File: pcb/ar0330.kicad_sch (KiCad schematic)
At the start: 37 parts

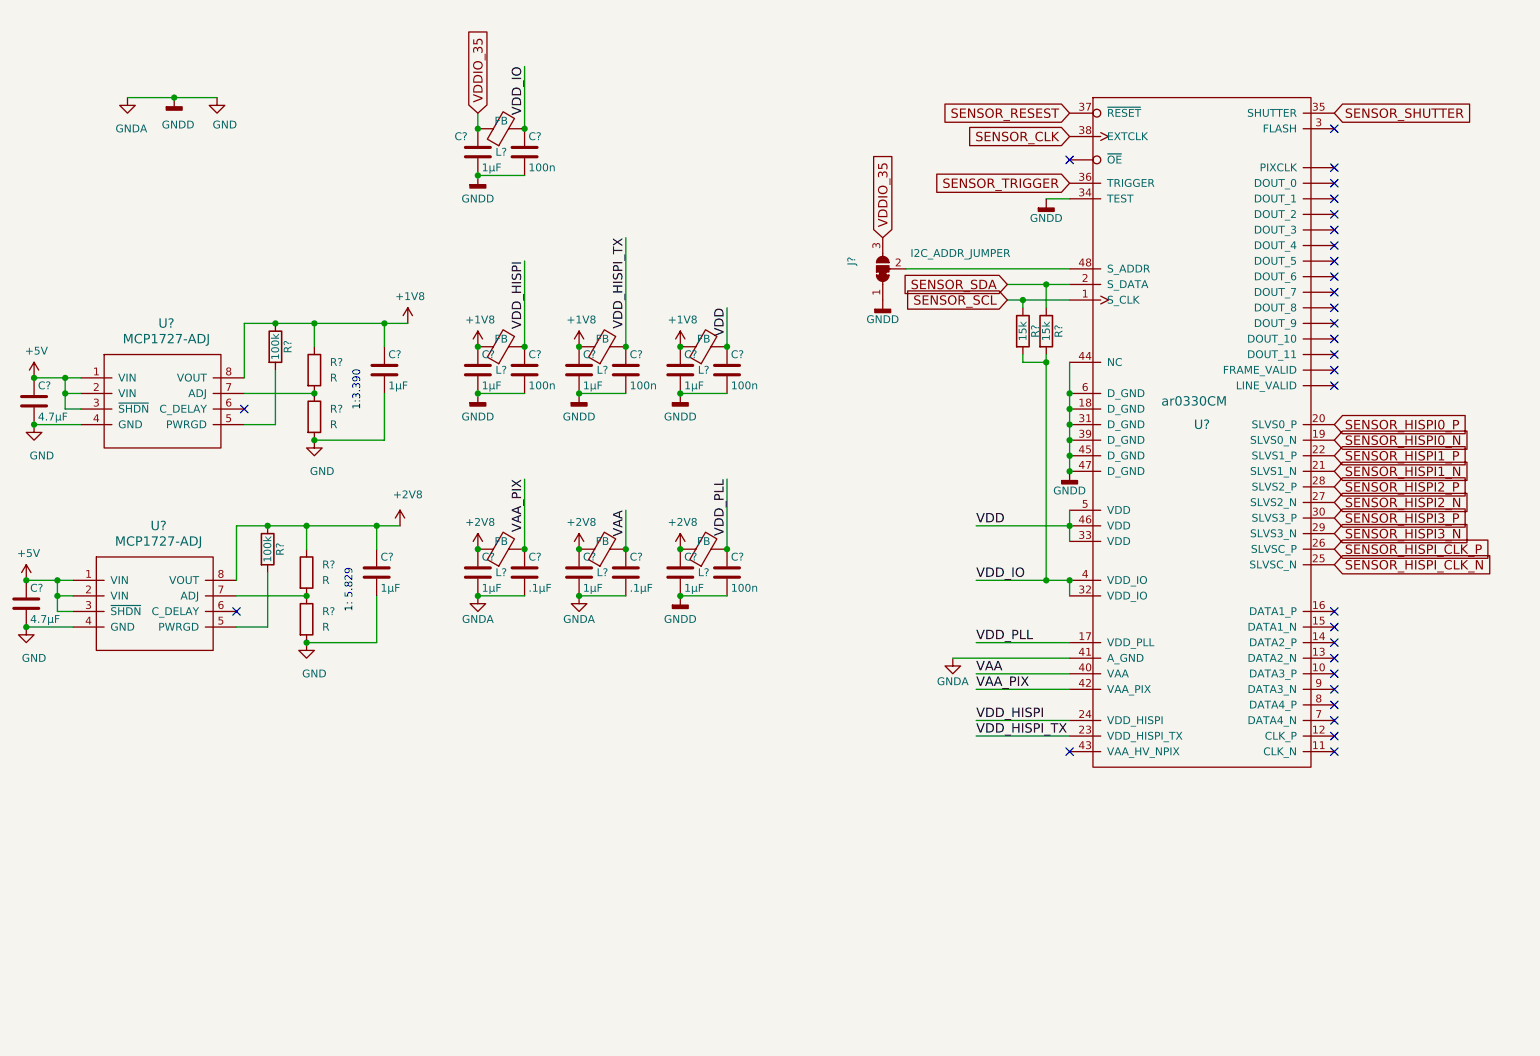
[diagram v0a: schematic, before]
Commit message: refinements; add ar1335 footprint
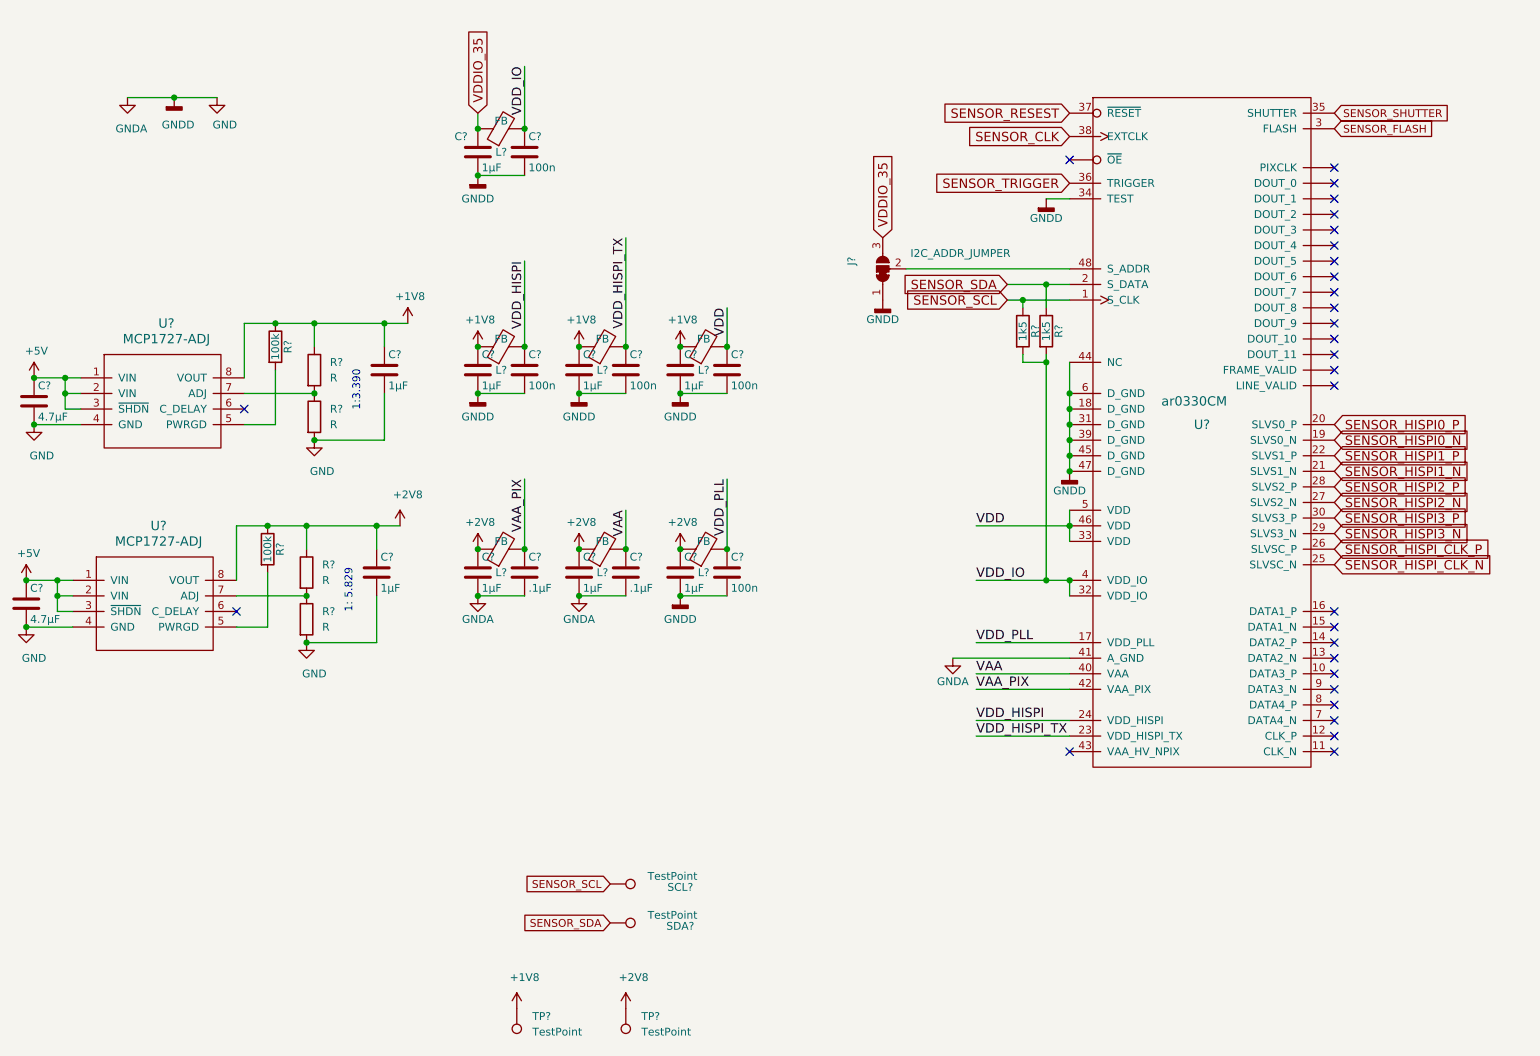
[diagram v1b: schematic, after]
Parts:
- added SCL?, SDA?: TestPoint, Connectors_TestPoints:Test_Point_Pad_2.0x2.0mm, symbol Connector:TestPoint
- added TP? (x2): TestPoint, symbol Connector:TestPoint
- R? (x2): value 15k -> 1k5
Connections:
- net +1V8: now also TP?.1
- net +2V8: now also TP?.1
- net SENSOR_SCL: now also SCL?.1
- net SENSOR_SDA: now also SDA?.1
- net SENSOR_FLASH: now reaches U?.3 (FLASH)
- no-connect marks 30 -> 29
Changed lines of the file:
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@@
   (no_connect (at 196.85 43.18))
   (no_connect (at 196.85 139.7))
-  (no_connect (at 240.03 38.1))
   (no_connect (at 240.03 44.45))
   (no_connect (at 240.03 46.99))
@@
     (effects (font (size 1.524 1.524)) (justify left))
   )
+  (global_label "SENSOR_SCL" (shape input) (at 121.92 161.29 180)    (property "Intersheet References" "${INTERSHEET_REFS}" (id 0) (at 106.0086 161.2106 0)
+      (effects (font (size 1.27 1.27)) (justify right) hide)
+    )
+    (effects (font (size 1.27 1.27)) (justify right))
+  )
+  (global_label "SENSOR_SDA" (shape input) (at 121.92 167.64 180)    (property "Intersheet References" "${INTERSHEET_REFS}" (id 0) (at 105.9481 167.5606 0)
+      (effects (font (size 1.27 1.27)) (justify right) hide)
+    )
+    (effects (font (size 1.27 1.27)) (justify right))
+  )
   (global_label "VDDIO_35" (shape input) (at 166.37 55.88 90)    (property "Intersheet References" "${INTERSHEET_REFS}" (id 0) (at 200.66 -273.05 0)
       (effects (font (size 1.27 1.27)) hide)
@@
     (effects (font (size 1.524 1.524)) (justify right))
   )
-  (global_label "SENSOR_SHUTTER" (shape input) (at 240.03 35.56 0)    (property "Intersheet References" "${INTERSHEET_REFS}" (id 0) (at 264.7841 35.4648 0)
-      (effects (font (size 1.524 1.524)) (justify left) hide)
-    )
-    (effects (font (size 1.524 1.524)) (justify left))
+  (global_label "SENSOR_SHUTTER" (shape input) (at 240.03 35.56 0)    (property "Intersheet References" "${INTERSHEET_REFS}" (id 0) (at 260.6585 35.4806 0)
+      (effects (font (size 1.27 1.27)) (justify left) hide)
+    )
+    (effects (font (size 1.27 1.27)) (justify left))
+  )
+  (global_label "SENSOR_FLASH" (shape input) (at 240.03 38.1 0)    (property "Intersheet References" "${INTERSHEET_REFS}" (id 0) (at 258.179 38.0206 0)
+      (effects (font (size 1.27 1.27)) (justify left) hide)
+    )
+    (effects (font (size 1.27 1.27)) (justify left))
   )
   (global_label "SENSOR_HISPI0_P" (shape input) (at 240.03 86.36 0)    (property "Intersheet References" "${INTERSHEET_REFS}" (id 0) (at 265.0744 86.2648 0)
@@
     (effects (font (size 1.524 1.524)) (justify left))
   )
+  (symbol (lib_id "Connector:TestPoint") (at 106.68 181.61 180) (unit 1)
+    (in_bom yes) (on_board yes)
+    (property "Reference" "TP?" (id 0) (at 109.22 182.88 0)
+      (effects (font (size 1.27 1.27)) (justify right))
+    )
+    (property "Value" "TestPoint" (id 1) (at 109.22 185.42 0)
+      (effects (font (size 1.27 1.27)) (justify right))
+    )
+    (property "Footprint" "" (id 2) (at 101.6 181.61 0)
+      (effects (font (size 1.27 1.27)) hide)
+    )
+    (property "Datasheet" "~" (id 3) (at 101.6 181.61 0)
+      (effects (font (size 1.27 1.27)) hide)
+    )
+  )
+  (symbol (lib_id "Connector:TestPoint") (at 121.92 161.29 270) (unit 1)
+    (in_bom yes) (on_board yes)
+    (property "Reference" "SCL?" (id 0) (at 133.35 162.56 90)
+      (effects (font (size 1.27 1.27)) (justify bottom))
+    )
+    (property "Value" "TestPoint" (id 1) (at 132.08 160.02 90))
+    (property "Footprint" "Connectors_TestPoints:Test_Point_Pad_2.0x2.0mm" (id 2) (at 121.92 161.29 0)
+      (effects (font (size 1.27 1.27)) hide)
+    )
+    (property "Datasheet" "" (id 3) (at 121.92 161.29 0)
+      (effects (font (size 1.27 1.27)) hide)
+    )
+  )
+  (symbol (lib_id "Connector:TestPoint") (at 121.92 167.64 270) (unit 1)
+    (in_bom yes) (on_board yes)
+    (property "Reference" "SDA?" (id 0) (at 133.35 168.91 90)
+      (effects (font (size 1.27 1.27)) (justify bottom))
+    )
+    (property "Value" "TestPoint" (id 1) (at 132.08 166.37 90))
+    (property "Footprint" "Connectors_TestPoints:Test_Point_Pad_2.0x2.0mm" (id 2) (at 121.92 167.64 0)
+      (effects (font (size 1.27 1.27)) hide)
+    )
+    (property "Datasheet" "" (id 3) (at 121.92 167.64 0)
+      (effects (font (size 1.27 1.27)) hide)
+    )
+  )
+  (symbol (lib_id "Connector:TestPoint") (at 124.46 181.61 180) (unit 1)
+    (in_bom yes) (on_board yes)
+    (property "Reference" "TP?" (id 0) (at 127 182.88 0)
+      (effects (font (size 1.27 1.27)) (justify right))
+    )
+    (property "Value" "TestPoint" (id 1) (at 127 185.42 0)
+      (effects (font (size 1.27 1.27)) (justify right))
+    )
+    (property "Footprint" "" (id 2) (at 119.38 181.61 0)
+      (effects (font (size 1.27 1.27)) hide)
+    )
+    (property "Datasheet" "~" (id 3) (at 119.38 181.61 0)
+      (effects (font (size 1.27 1.27)) hide)
+    )
+  )
   (symbol (lib_id "power:+5V") (at 26.67 111.76 0) (unit 1)
     (in_bom yes) (on_board yes)
@@
     )
   )
+  (symbol (lib_id "power:+1V8") (at 106.68 181.61 0) (unit 1)
+    (in_bom yes) (on_board yes)
+    (property "Reference" "#PWR?" (id 0) (at 106.68 185.42 0)
+      (effects (font (size 1.27 1.27)) hide)
+    )
+    (property "Value" "+1V8" (id 1) (at 107.95 176.53 0))
+    (property "Footprint" "" (id 2) (at 106.68 181.61 0)
+      (effects (font (size 1.27 1.27)) hide)
+    )
+    (property "Datasheet" "" (id 3) (at 106.68 181.61 0)
+      (effects (font (size 1.27 1.27)) hide)
+    )
+  )
   (symbol (lib_id "power:+1V8") (at 116.84 73.66 0) (unit 1)
     (in_bom yes) (on_board yes)
@@
     )
     (property "Datasheet" "" (id 3) (at 116.84 106.68 0)
+      (effects (font (size 1.27 1.27)) hide)
+    )
+  )
+  (symbol (lib_id "power:+2V8") (at 124.46 181.61 0) (unit 1)
+    (in_bom yes) (on_board yes)
+    (property "Reference" "#PWR?" (id 0) (at 124.46 185.42 0)
+      (effects (font (size 1.27 1.27)) hide)
+    )
+    (property "Value" "+2V8" (id 1) (at 125.73 176.53 0))
+    (property "Footprint" "" (id 2) (at 124.46 181.61 0)
+      (effects (font (size 1.27 1.27)) hide)
+    )
+    (property "Datasheet" "" (id 3) (at 124.46 181.61 0)
       (effects (font (size 1.27 1.27)) hide)
     )
@@
     (in_bom yes) (on_board yes)
     (property "Reference" "R?" (id 0) (at 191.262 71.12 90))
-    (property "Value" "15k" (id 1) (at 189.23 71.12 90))
+    (property "Value" "1k5" (id 1) (at 189.23 71.12 90))
     (property "Footprint" "Resistors_SMD:R_0603_HandSoldering" (id 2) (at 187.452 71.12 90)
       (effects (font (size 1.27 1.27)) hide)
@@
     (in_bom yes) (on_board yes)
     (property "Reference" "R?" (id 0) (at 195.072 71.12 90))
-    (property "Value" "15k " (id 1) (at 193.04 71.12 90))
+    (property "Value" "1k5" (id 1) (at 193.04 71.12 90))
     (property "Footprint" "Resistors_SMD:R_0603_HandSoldering" (id 2) (at 191.262 71.12 90)
       (effects (font (size 1.27 1.27)) hide)

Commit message: Change Plans: two image sensors
* Redo power management
* Add level shifters
* Intention to use both image sensors on the same board
* Add Pmod & LEDs
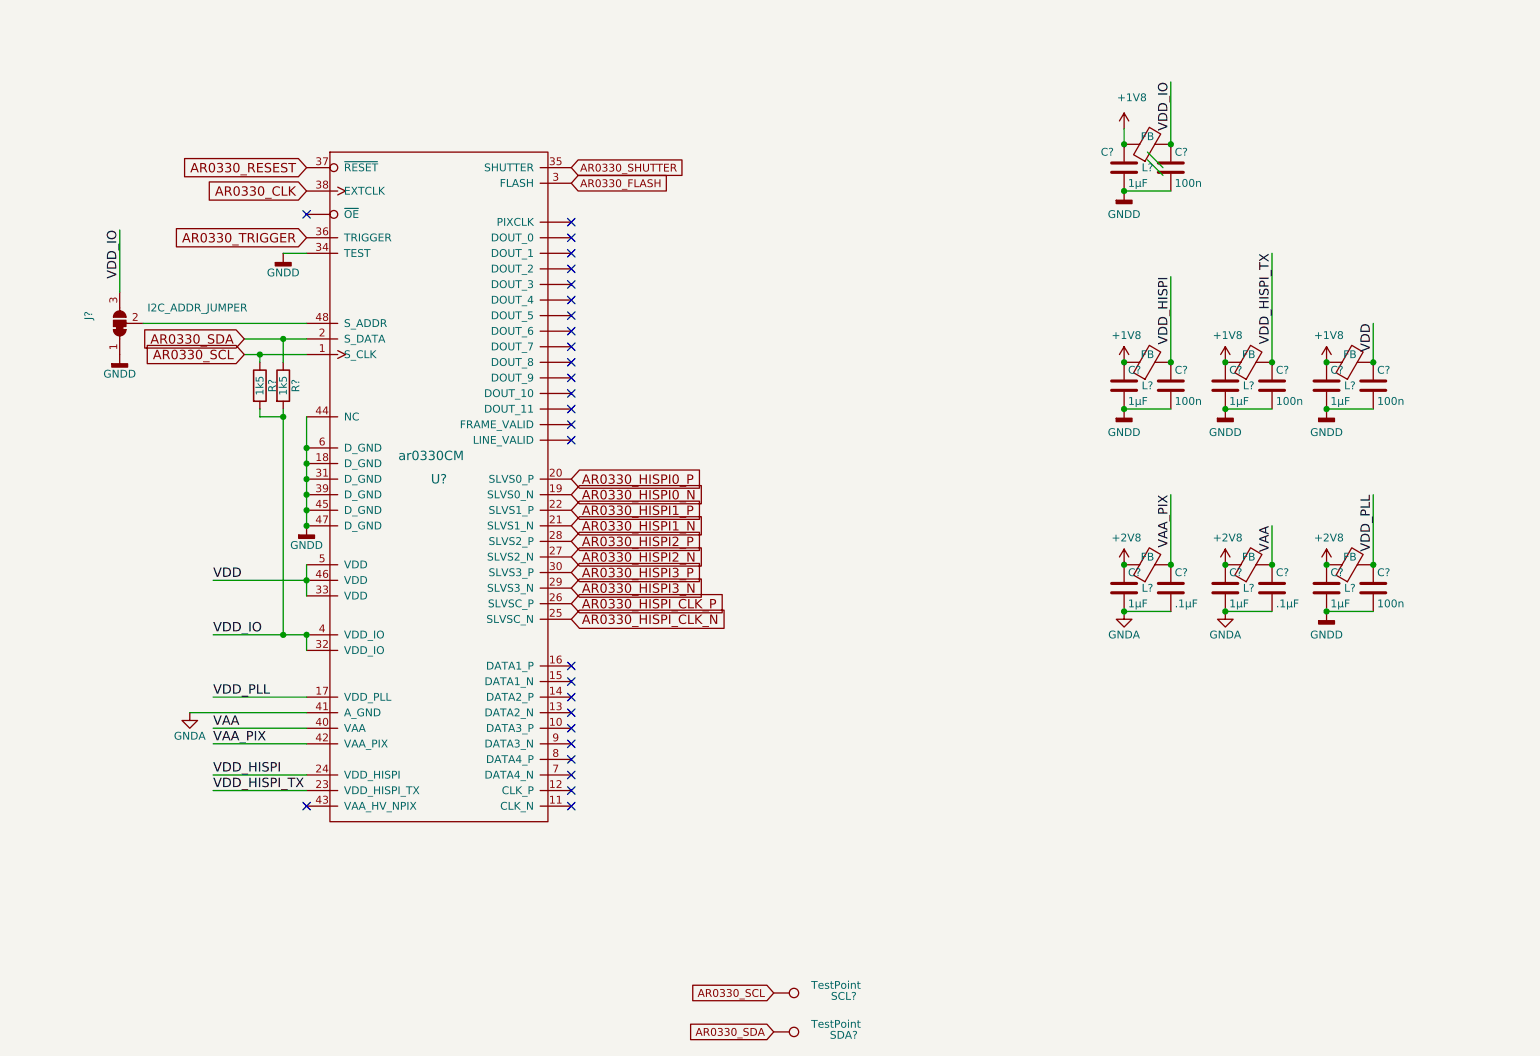
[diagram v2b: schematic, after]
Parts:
- removed C? (x2): 1µF, Capacitors_SMD:C_0402, symbol Device:C
- removed C? (x2): 4.7µF, Capacitors_SMD:C_0603_HandSoldering, symbol Device:C
- removed R? (x2): 100k, Resistors_SMD:R_0603_HandSoldering, symbol Device:R
- removed R? (x4): R, symbol Device:R
- removed TP? (x2): TestPoint, symbol Connector:TestPoint
- removed U? (x2): MCP1727-ADJ, symbol parts:MCP1727-ADJ
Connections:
- net +1V8: now also C?.1, L?.1
- net VDD_IO: now also J?.3 (B)
- net GND renamed GNDD
- net GNDD: no longer C?.2, C?.2, C?.2, C?.2, U?.41 (A_GND)
- net SENSOR_CLK renamed AR0330_CLK
- net SENSOR_FLASH renamed AR0330_FLASH
- net SENSOR_HISPI0_N renamed AR0330_HISPI0_N
- net SENSOR_HISPI0_P renamed AR0330_HISPI0_P
- net SENSOR_HISPI1_N renamed AR0330_HISPI1_N
- net SENSOR_HISPI1_P renamed AR0330_HISPI1_P
- net SENSOR_HISPI2_N renamed AR0330_HISPI2_N
- net SENSOR_HISPI2_P renamed AR0330_HISPI2_P
- net SENSOR_HISPI3_N renamed AR0330_HISPI3_N
- net SENSOR_HISPI3_P renamed AR0330_HISPI3_P
- net SENSOR_HISPI_CLK_N renamed AR0330_HISPI_CLK_N
- net SENSOR_HISPI_CLK_P renamed AR0330_HISPI_CLK_P
- net SENSOR_RESEST renamed AR0330_RESEST
- net SENSOR_SCL renamed AR0330_SCL
- net SENSOR_SDA renamed AR0330_SDA
- net SENSOR_SHUTTER renamed AR0330_SHUTTER
- net SENSOR_TRIGGER renamed AR0330_TRIGGER
- removed net VDDIO_35: C?.1, J?.3 (B), L?.1
- new net GNDA: C?.2, C?.2, C?.2, C?.2, U?.41 (A_GND)
- no-connect marks 29 -> 27
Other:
- note removed: "1: 5.829"
- note removed: "1:3.390"
- moved on the sheet: C?, J?, L?, R?, SCL?, SDA?, U?

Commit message: add i2c addresses
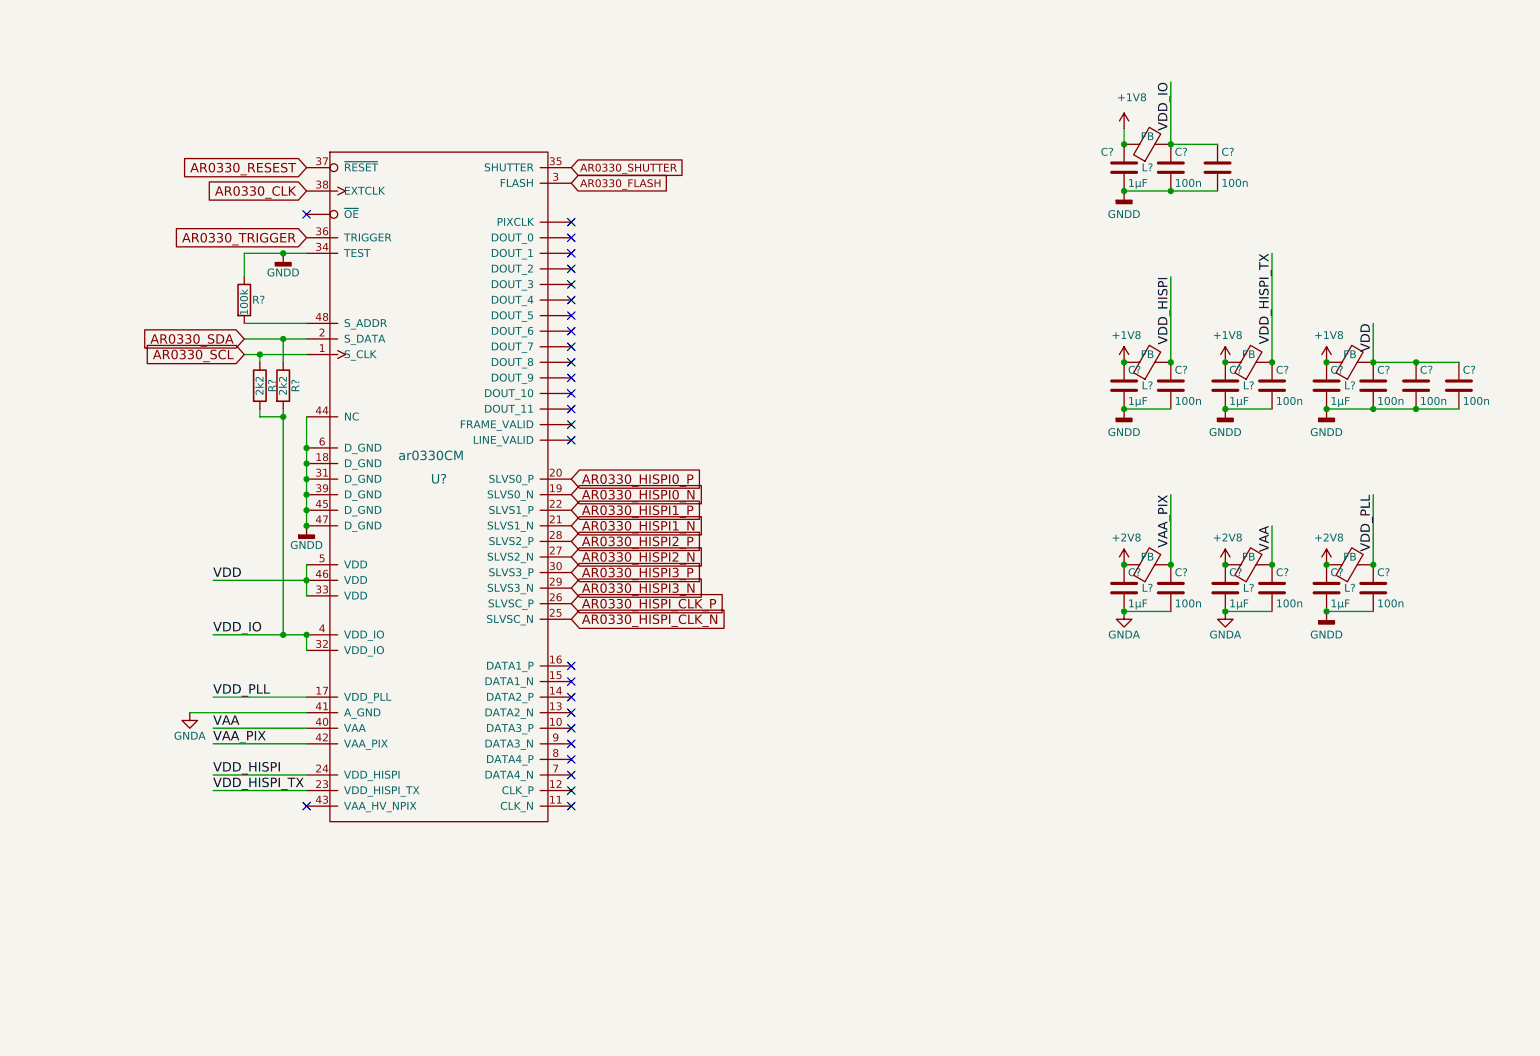
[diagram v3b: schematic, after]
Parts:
- removed J?: I2C_ADDR_JUMPER, Connectors:GS3, symbol Jumper:SolderJumper_3_Bridged12
- removed SCL?, SDA?: TestPoint, Connectors_TestPoints:Test_Point_Pad_2.0x2.0mm, symbol Connector:TestPoint
- added C? (x3): 100n, Capacitors_SMD:C_0402, symbol Device:C
- added R?: 100k, symbol Device:R
- C? (x2): value .1µF -> 100n
- R? (x2): value 1k5 -> 2k2
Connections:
- net GNDD: now also C?.2, C?.2, C?.2, R?.1
- net VDD: now also C?.1, C?.1
- net VDD_IO: now also C?.1
- net at U?.48 (S_ADDR): now also R?.2
